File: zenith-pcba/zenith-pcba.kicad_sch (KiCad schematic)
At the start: 2 parts, among them U1 XC7A50T-CSG325, U2 K4B4G1646E-BCNB

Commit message: feat(pcba): initial programmer setup
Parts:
- removed U1: XC7A50T-CSG325, Package_BGA:Xilinx_CSG325, symbol FPGA_Xilinx_Artix7:XC7A50T-CSG325
- removed U2: K4B4G1646E-BCNB, BGA96_K4B4G1_SAM, symbol K4B4G1646E-BCNB:K4B4G1646E-BCNB
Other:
- added sheet Programmer (programmerrealkicad_sch.kicad_sch)
- added sheet TODO (todo.kicad_sch)
- added sheet TODOP (todop.kicad_sch)

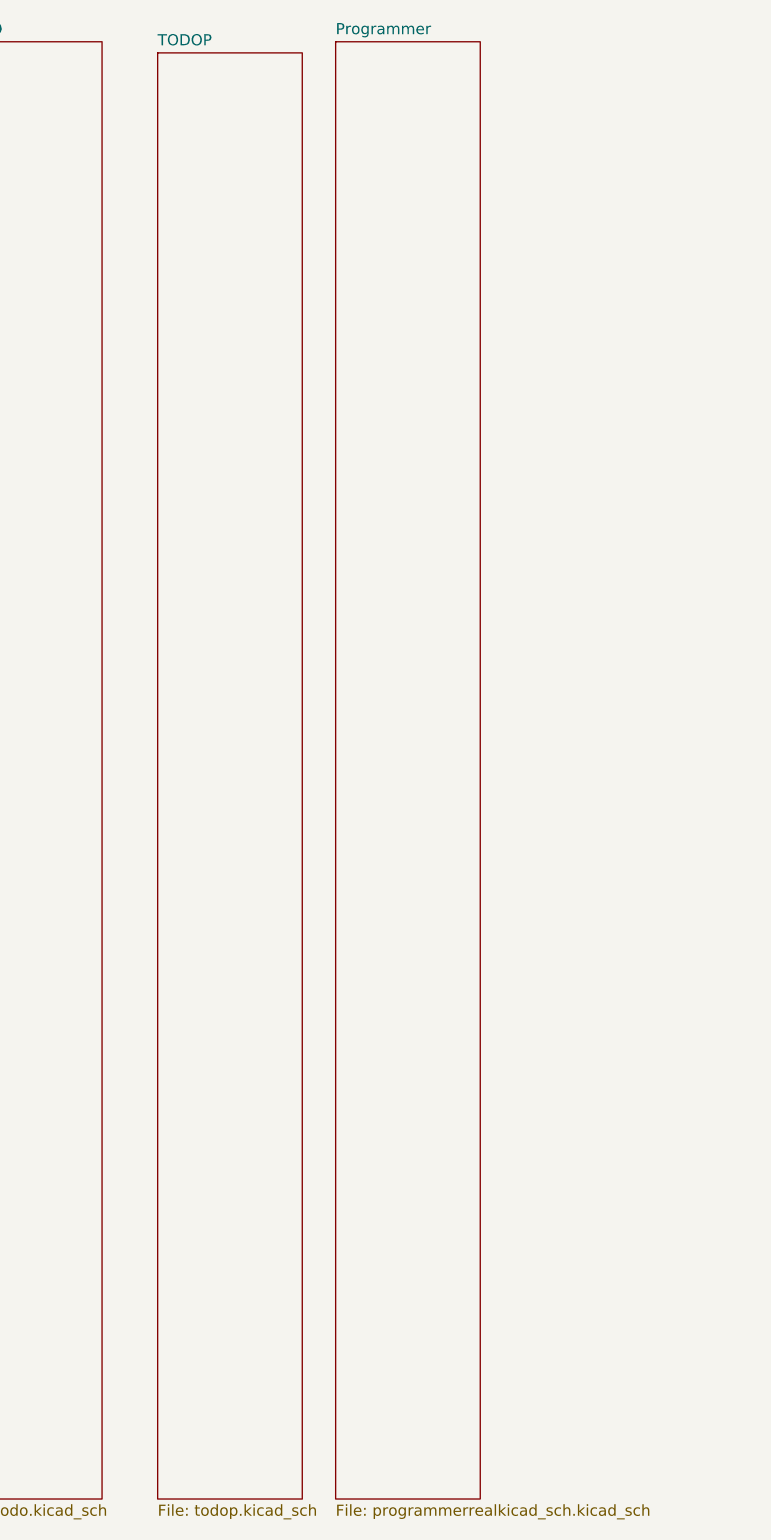
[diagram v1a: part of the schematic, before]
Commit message: feat(pcba): sd card schematic
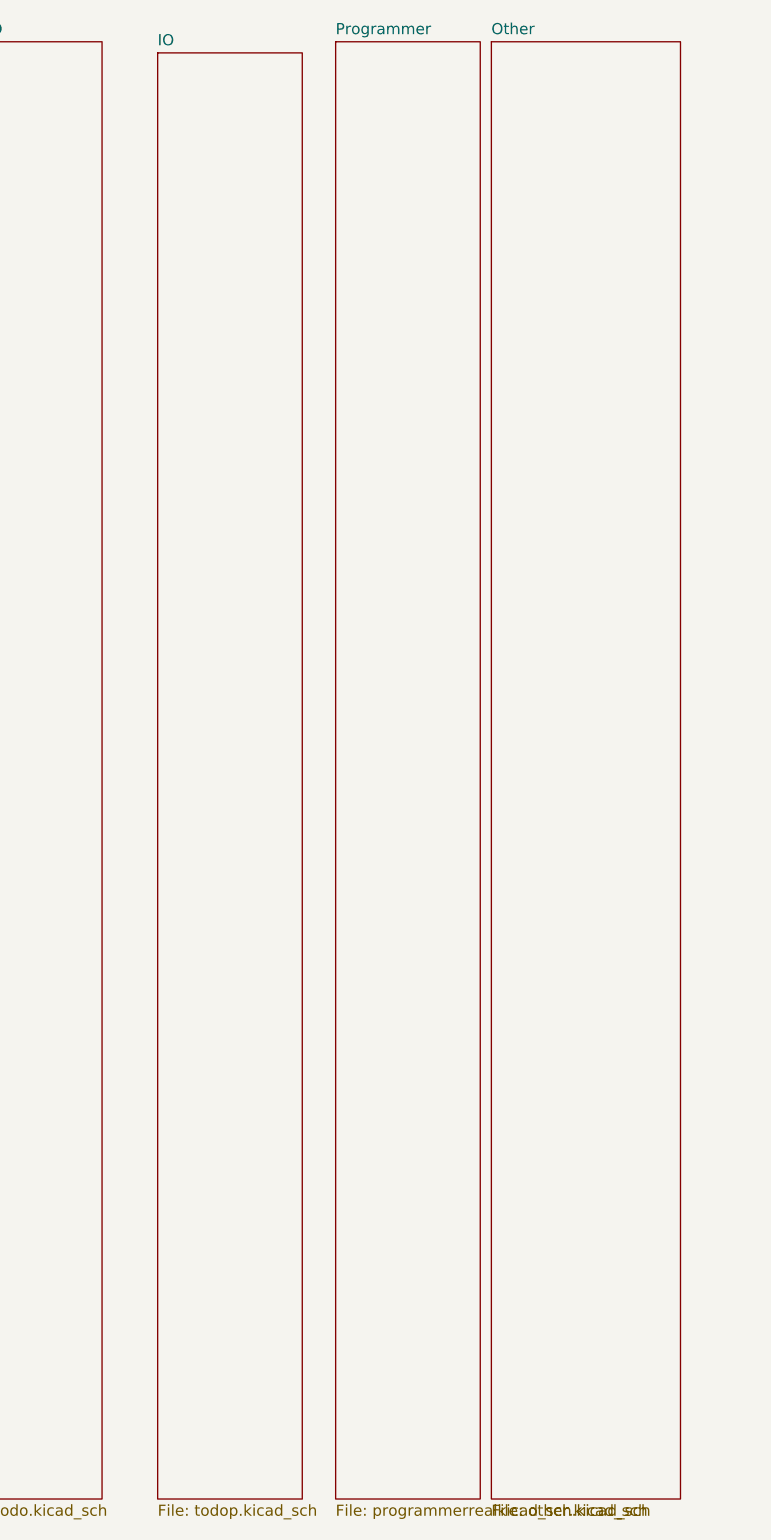
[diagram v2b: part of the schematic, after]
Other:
- sheet TODOP renamed IO
- added sheet Other (other.kicad_sch)
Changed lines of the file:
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@@
 	(paper "A4")
+	(sheet
+		(at 82.55 20.32)
+		(size 21.59 166.37)
+		(exclude_from_sim no)
+		(in_bom yes)
+		(on_board yes)
+		(dnp no)
+		(fields_autoplaced yes)
+		(stroke
+			(width 0.1524)
+			(type solid)
+		)
+		(fill
+			(color 0 0 0 0)
+		)
+		(property "Sheetname" "Other"
+			(at 82.55 19.6084 0)
+			(show_name no)
+			(do_not_autoplace no)
+			(effects
+				(font
+					(size 1.27 1.27)
+				)
+				(justify left bottom)
+			)
+		)
+		(property "Sheetfile" "other.kicad_sch"
+			(at 82.55 187.2746 0)
+			(show_name no)
+			(do_not_autoplace no)
+			(effects
+				(font
+					(size 1.27 1.27)
+				)
+				(justify left top)
+			)
+		)
+		(instances
+			(project "zenith-pcba"
+				(path "/998c5703-2ef0-4484-8ced-1d53dcc65d39"
+					(page "5")
+				)
+			)
+		)
+	)
 	(sheet
 		(at 21.59 20.32)
@@
 			(color 0 0 0 0)
 		)
-		(property "Sheetname" "TODOP"
+		(property "Sheetname" "IO"
 			(at 44.45 20.8784 0)
 			(show_name no)

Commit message: chore(pcba): clean up pages
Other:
- added sheet Disconnected IO (disconnected_io.kicad_sch)
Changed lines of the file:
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@@
 	(paper "A4")
 	(sheet
-		(at 82.55 20.32)
+		(at 66.04 24.13)
+		(size 20.32 161.29)
+		(exclude_from_sim no)
+		(in_bom yes)
+		(on_board yes)
+		(dnp no)
+		(fields_autoplaced yes)
+		(stroke
+			(width 0.1524)
+			(type solid)
+		)
+		(fill
+			(color 0 0 0 0)
+		)
+		(property "Sheetname" "Disconnected IO"
+			(at 66.04 23.4184 0)
+			(show_name no)
+			(do_not_autoplace no)
+			(effects
+				(font
+					(size 1.27 1.27)
+				)
+				(justify left bottom)
+			)
+		)
+		(property "Sheetfile" "disconnected_io.kicad_sch"
+			(at 66.04 186.0046 0)
+			(show_name no)
+			(do_not_autoplace no)
+			(effects
+				(font
+					(size 1.27 1.27)
+				)
+				(justify left top)
+			)
+		)
+		(instances
+			(project "zenith-pcba"
+				(path "/998c5703-2ef0-4484-8ced-1d53dcc65d39"
+					(page "4")
+				)
+			)
+		)
+	)
+	(sheet
+		(at 121.92 22.86)
 		(size 21.59 166.37)
 		(exclude_from_sim no)
@@
 		)
 		(property "Sheetname" "Other"
-			(at 82.55 19.6084 0)
+			(at 121.92 22.1484 0)
 			(show_name no)
 			(do_not_autoplace no)
@@
 		)
 		(property "Sheetfile" "other.kicad_sch"
-			(at 82.55 187.2746 0)
-			(show_name no)
-			(do_not_autoplace no)
-			(effects
-				(font
-					(size 1.27 1.27)
-				)
-				(justify left top)
-			)
-		)
-		(instances
-			(project "zenith-pcba"
-				(path "/998c5703-2ef0-4484-8ced-1d53dcc65d39"
-					(page "5")
+			(at 121.92 189.8146 0)
+			(show_name no)
+			(do_not_autoplace no)
+			(effects
+				(font
+					(size 1.27 1.27)
+				)
+				(justify left top)
+			)
+		)
+		(instances
+			(project "zenith-pcba"
+				(path "/998c5703-2ef0-4484-8ced-1d53dcc65d39"
+					(page "6")
 				)
 			)
@@
 	)
 	(sheet
-		(at 64.77 20.32)
+		(at 104.14 22.86)
 		(size 16.51 166.37)
 		(exclude_from_sim no)
@@
 		)
 		(property "Sheetname" "Programmer"
-			(at 64.77 19.6084 0)
+			(at 104.14 22.1484 0)
 			(show_name no)
 			(do_not_autoplace no)
@@
 		)
 		(property "Sheetfile" "programmerrealkicad_sch.kicad_sch"
-			(at 64.77 187.2746 0)
-			(show_name no)
-			(do_not_autoplace no)
-			(effects
-				(font
-					(size 1.27 1.27)
-				)
-				(justify left top)
-			)
-		)
-		(instances
-			(project "zenith-pcba"
-				(path "/998c5703-2ef0-4484-8ced-1d53dcc65d39"
-					(page "4")
-				)
-			)
+			(at 104.14 189.8146 0)
+			(show_name no)
+			(do_not_autoplace no)
+			(effects
+				(font
+					(size 1.27 1.27)
+				)
+				(justify left top)
+			)
+		)
+		(instances
+			(project "zenith-pcba"
+				(path "/998c5703-2ef0-4484-8ced-1d53dcc65d39"
+					(page "5")
+				)
+			)
